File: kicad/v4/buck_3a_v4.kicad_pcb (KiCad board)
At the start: 2 copper layers, 44 x 44 mm, 27 parts, among them J3 Conn_01x04, J5 Conn_01x06, Q1 BSC022N04LSATMA, U1 MAX16820ATT, U2 ATtiny45-20SU

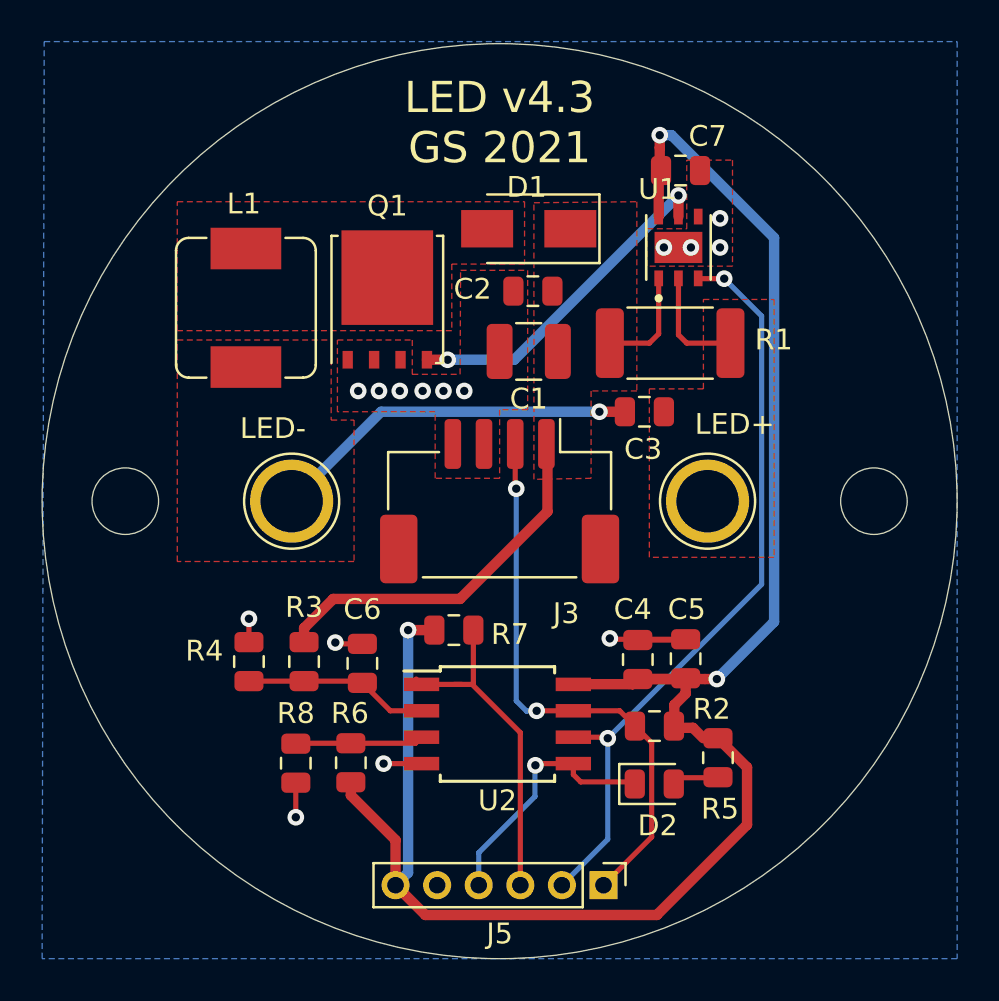
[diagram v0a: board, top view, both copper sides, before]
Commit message: change kicad folder
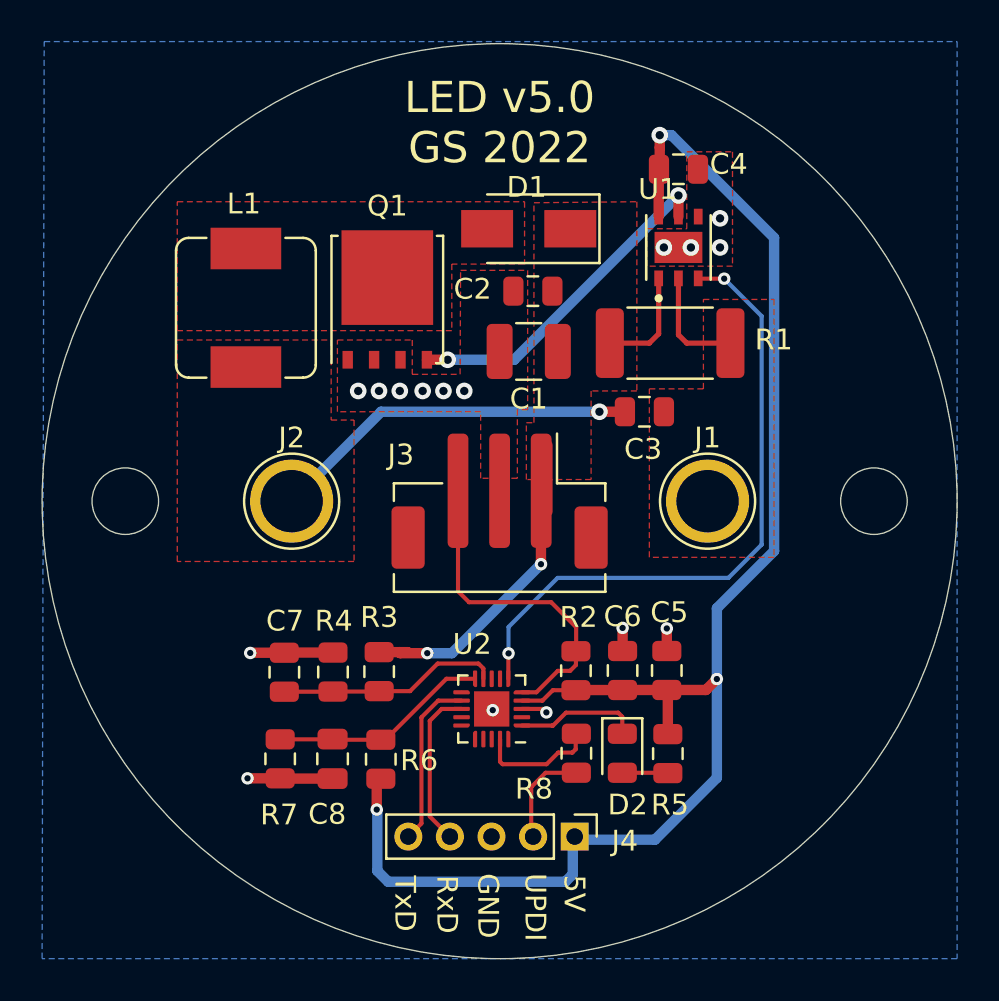
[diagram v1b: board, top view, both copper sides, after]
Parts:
- removed J5: Conn_01x06, Connector_PinHeader_2.00mm:PinHeader_1x06_P2.00mm_Vertical
- removed LED+: LED+, TestPoint:TestPoint_Plated_Hole_D3.0mm
- removed LED-: LED-, TestPoint:TestPoint_Plated_Hole_D3.0mm
- added C8: 4n70, Capacitor_SMD:C_0805_2012Metric, F.Cu at (42.0, 62.4)
- added J1: LED+, TestPoint:TestPoint_Plated_Hole_D3.0mm, F.Cu at (60.0, 50.0)
- added J2: LED-, TestPoint:TestPoint_Plated_Hole_D3.0mm, F.Cu at (40.0, 50.0)
- added J4: Conn_01x05, Connector_PinHeader_2.00mm:PinHeader_1x05_P2.00mm_Vertical, F.Cu at (53.6, 66.1)
- C1: value 100u/16V -> 22u0 / 25V
- C4: value 22u0/16V -> 22u0 / 25V
- C5: value 100n -> 22u0 / 25V
- C6: value 4n70 -> 100n
- C7: value 22u0/16V -> 4n70
- J3: value Conn_01x04 -> JST_B3B-PH-SM4-TB(LF)(SN); footprint Connector_JST:JST_ZE_BM04B-ZESS-TBT_1x04-1MP_P1.50mm_Vertical -> Connector_JST:JST_PH_B3B-PH-SM4-TB_1x03-1MP_P2.00mm_Vertical
- R7: value 10k0 -> CMFB103F3950FANT
- R8: value CMFB103F3950FANT -> 470r
- U2: value ATtiny45-20SU -> ATtiny1616-M; footprint Package_SO:SOIJ-8_5.3x5.3mm_P1.27mm -> Package_DFN_QFN:VQFN-20-1EP_3x3mm_P0.4mm_EP1.7x1.7mm
- moved C7 30.7 mm to (39.6, 58.2), turned to 90 degrees
- moved C4 23.7 mm to (58.6, 34.0), turned to 0 degrees
- moved R8 13.5 mm to (53.7, 62.1)
- moved C6 12.5 mm to (55.9, 58.1)
- moved R7 10.4 mm to (39.4, 62.4), turned to -90 degrees
- moved R2 4.62 mm to (53.7, 58.2), turned to 90 degrees
- moved R4 4.07 mm to (42.0, 58.2)
- moved R3 3.64 mm to (44.2, 58.2)
- moved R5 2.42 mm to (58.1, 62.1)
- moved D2 2.13 mm to (55.9, 62.1), turned to -90 degrees
- moved R6 1.45 mm to (44.3, 62.4)
- moved C5 1.07 mm to (58.0, 58.1)
- moved U2 0.78 mm to (49.6, 60.0), turned to 180 degrees
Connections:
- C6 pad 1: /VMESS -> +5V
- C7 pad 1: +5V -> /VMESS
- J3 pad 2: /MODE -> GND
- J3 pad 3: GND -> /MODE
- R7 pad 1: +5V -> /TMESS
- R7 pad 2: /RESET -> GND
- R8 pad 1: /TMESS -> Net-(R8-Pad1)
- R8 pad 2: GND -> Net-(J4-Pad2)
- U2 pad 1: /RESET -> /LED
- U2 pad 2: /VMESS -> unconnected-(U2-Pad2)
- U2 pad 3: /TMESS -> GND
- U2 pad 4: GND -> +5V
- U2 pad 5: /LED -> /MODE
- U2 pad 7: /MODE -> unconnected-(U2-Pad7)
- U2 pad 8: +5V -> unconnected-(U2-Pad8)
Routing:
- net +5V: track 92.1 -> 74.7 mm
- net /RESET: track 16.4 -> 0.00 mm
- net /MODE: track 27.5 -> 16.2 mm, vias 2 -> 0
- net /TXD: track 0.00 -> 8.38 mm
- net /RXD: track 0.00 -> 7.73 mm
- net /LED: track 12.0 -> 6.00 mm, vias 1 -> 0
- net Net-(R8-Pad1): track 0.00 -> 5.82 mm
- net /PWM: track 36.8 -> 31.1 mm
- net Net-(J4-Pad2): track 0.00 -> 4.84 mm
- net /TMESS: track 6.18 -> 10.7 mm
- net /VMESS: track 8.89 -> 10.7 mm
- net VCC: track 23.2 -> 22.0 mm, vias 0 -> 2
- net GND: track 12.0 -> 11.8 mm, vias 15 -> 16
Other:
- board text added: "5V"
- board text added: "GND"
- board text added: "LED v5.0 GS 2022"
- board text added: "RxD"
- board text added: "TxD"
- board text added: "UPDI"
- board text removed: "LED v4.3 GS 2021"
